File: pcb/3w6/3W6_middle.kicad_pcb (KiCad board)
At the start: 2 copper layers, 243.2 x 106 mm, 8 parts

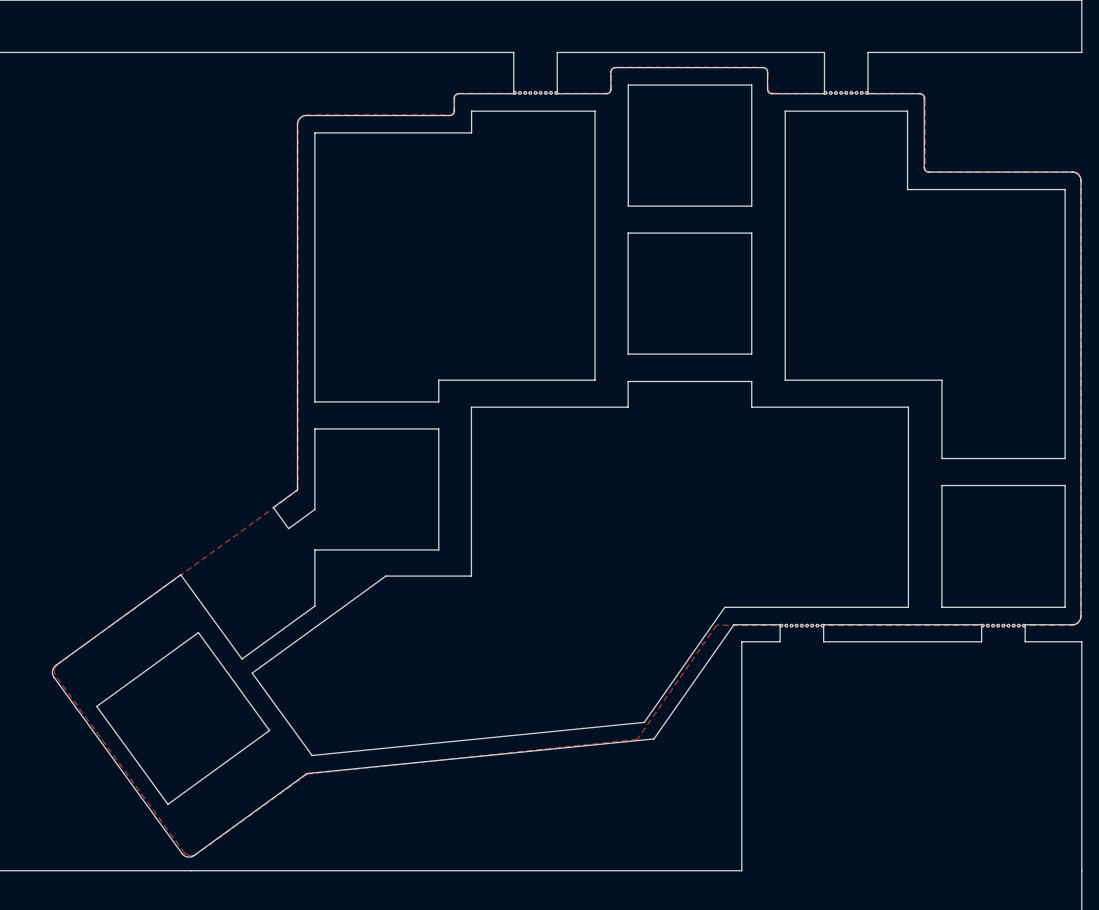
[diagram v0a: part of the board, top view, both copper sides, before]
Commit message: fix middle plate outlines right half
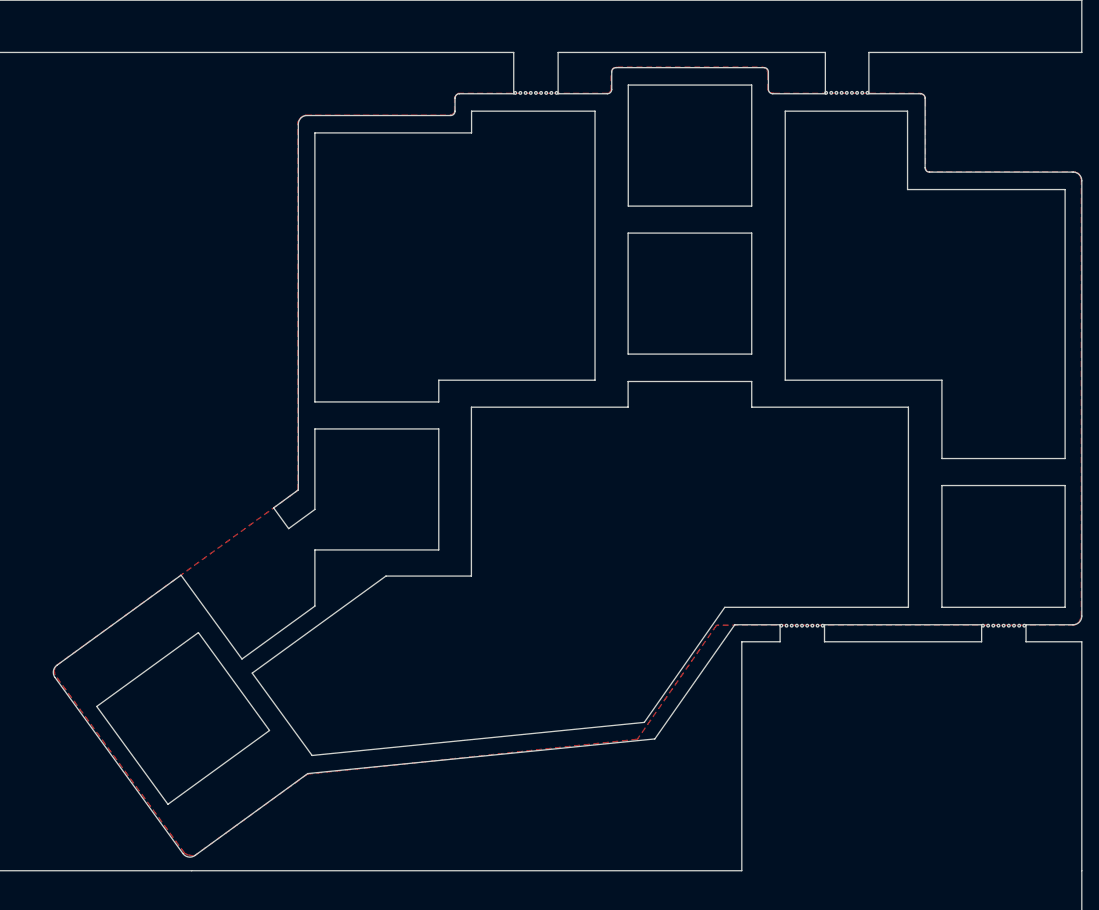
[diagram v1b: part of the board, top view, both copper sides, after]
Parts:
- removed the REF** at (253.4, 90.5)
- removed the REF** at (258.5, 29.2)
- added REF**: Breakaway_Tabs, kbd:Breakaway_Tabs, F.Cu at (253.4, 90.5)
- added REF**: Breakaway_Tabs, kbd:Breakaway_Tabs, F.Cu at (258.6, 29.2)
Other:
- outline, holes or cut-outs redrawn
